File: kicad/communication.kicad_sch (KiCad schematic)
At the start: 5 parts

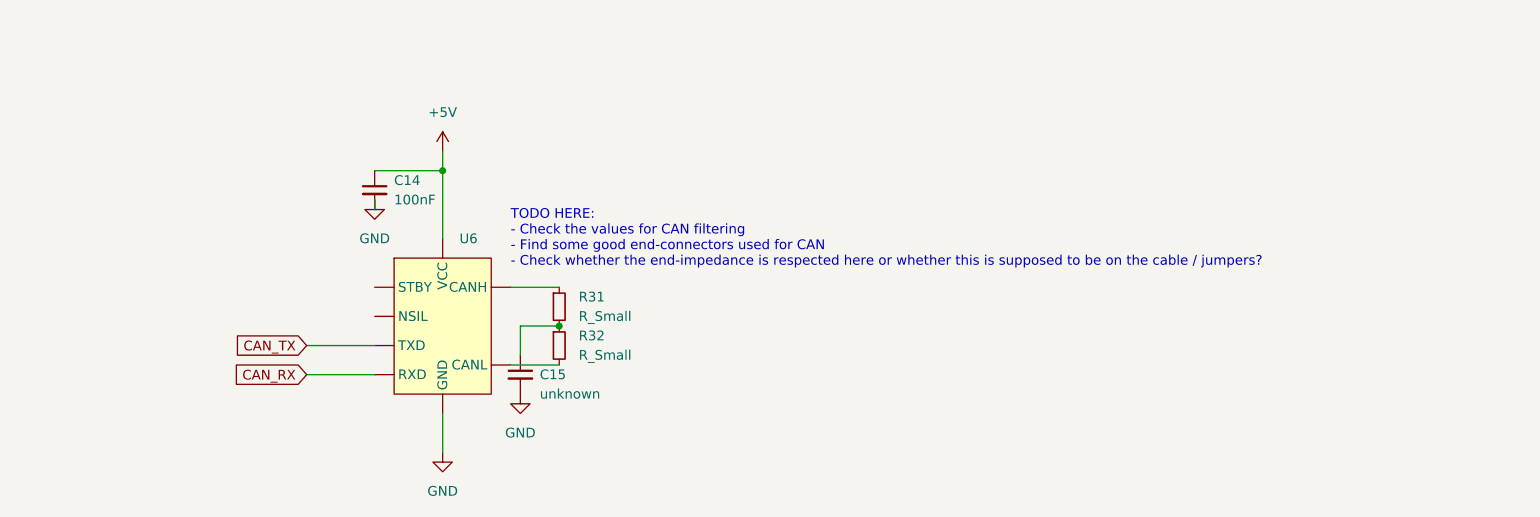
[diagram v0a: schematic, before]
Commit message: [kicad] Added end-connector and differential resistnace
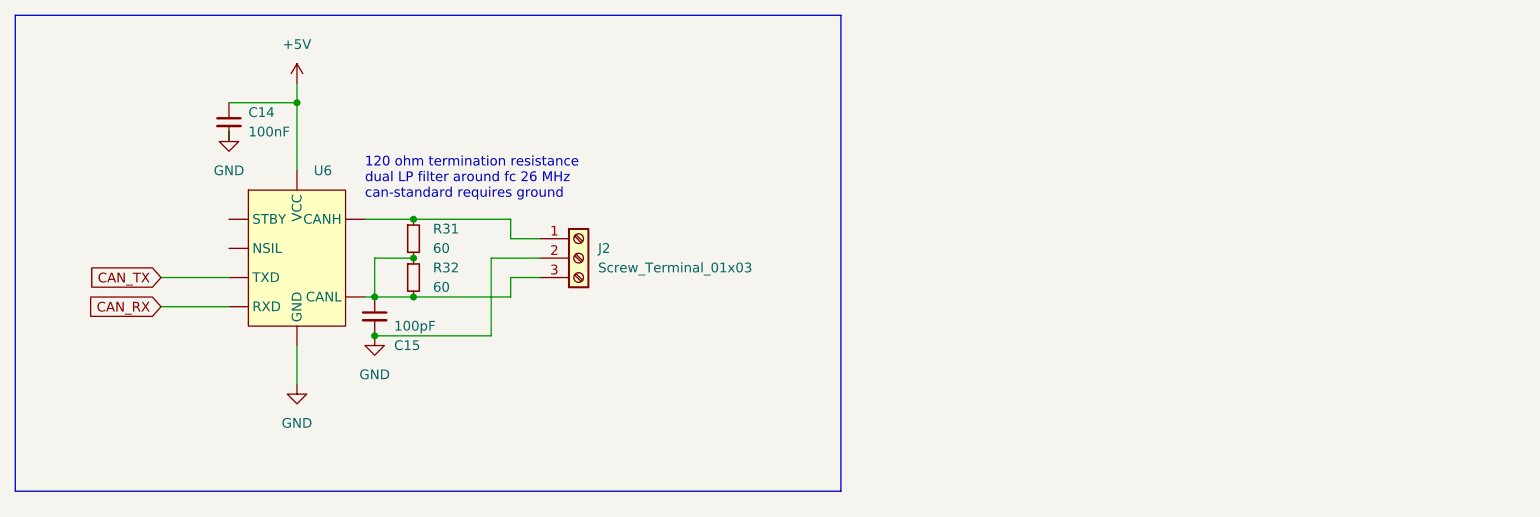
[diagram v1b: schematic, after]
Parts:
- added J2: Screw_Terminal_01x03, symbol Connector:Screw_Terminal_01x03
- C15: value unknown -> 100pF
- R31, R32: value R_Small -> 60
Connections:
- net GND: now also J2.2 (Pin_2)
- net at R31.1, U6. (VCC): now also J2.1 (Pin_1)
- net at C15.1, R31.2, R32.1: now also R32.2, U6. (VCC), J2.3 (Pin_3)
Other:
- note added: "120 ohm termination resistance dual LP filter around fc 26 MHz can-standard requires ground"
- note removed: "TODO HERE: - Check the values for CAN filtering - Find some good end-connectors used for CAN - Check whether the end-impedance is respected here or whether this is supposed to be on the cable / jumpers?"
- moved on the sheet: C14, C15, R31, R32, U6

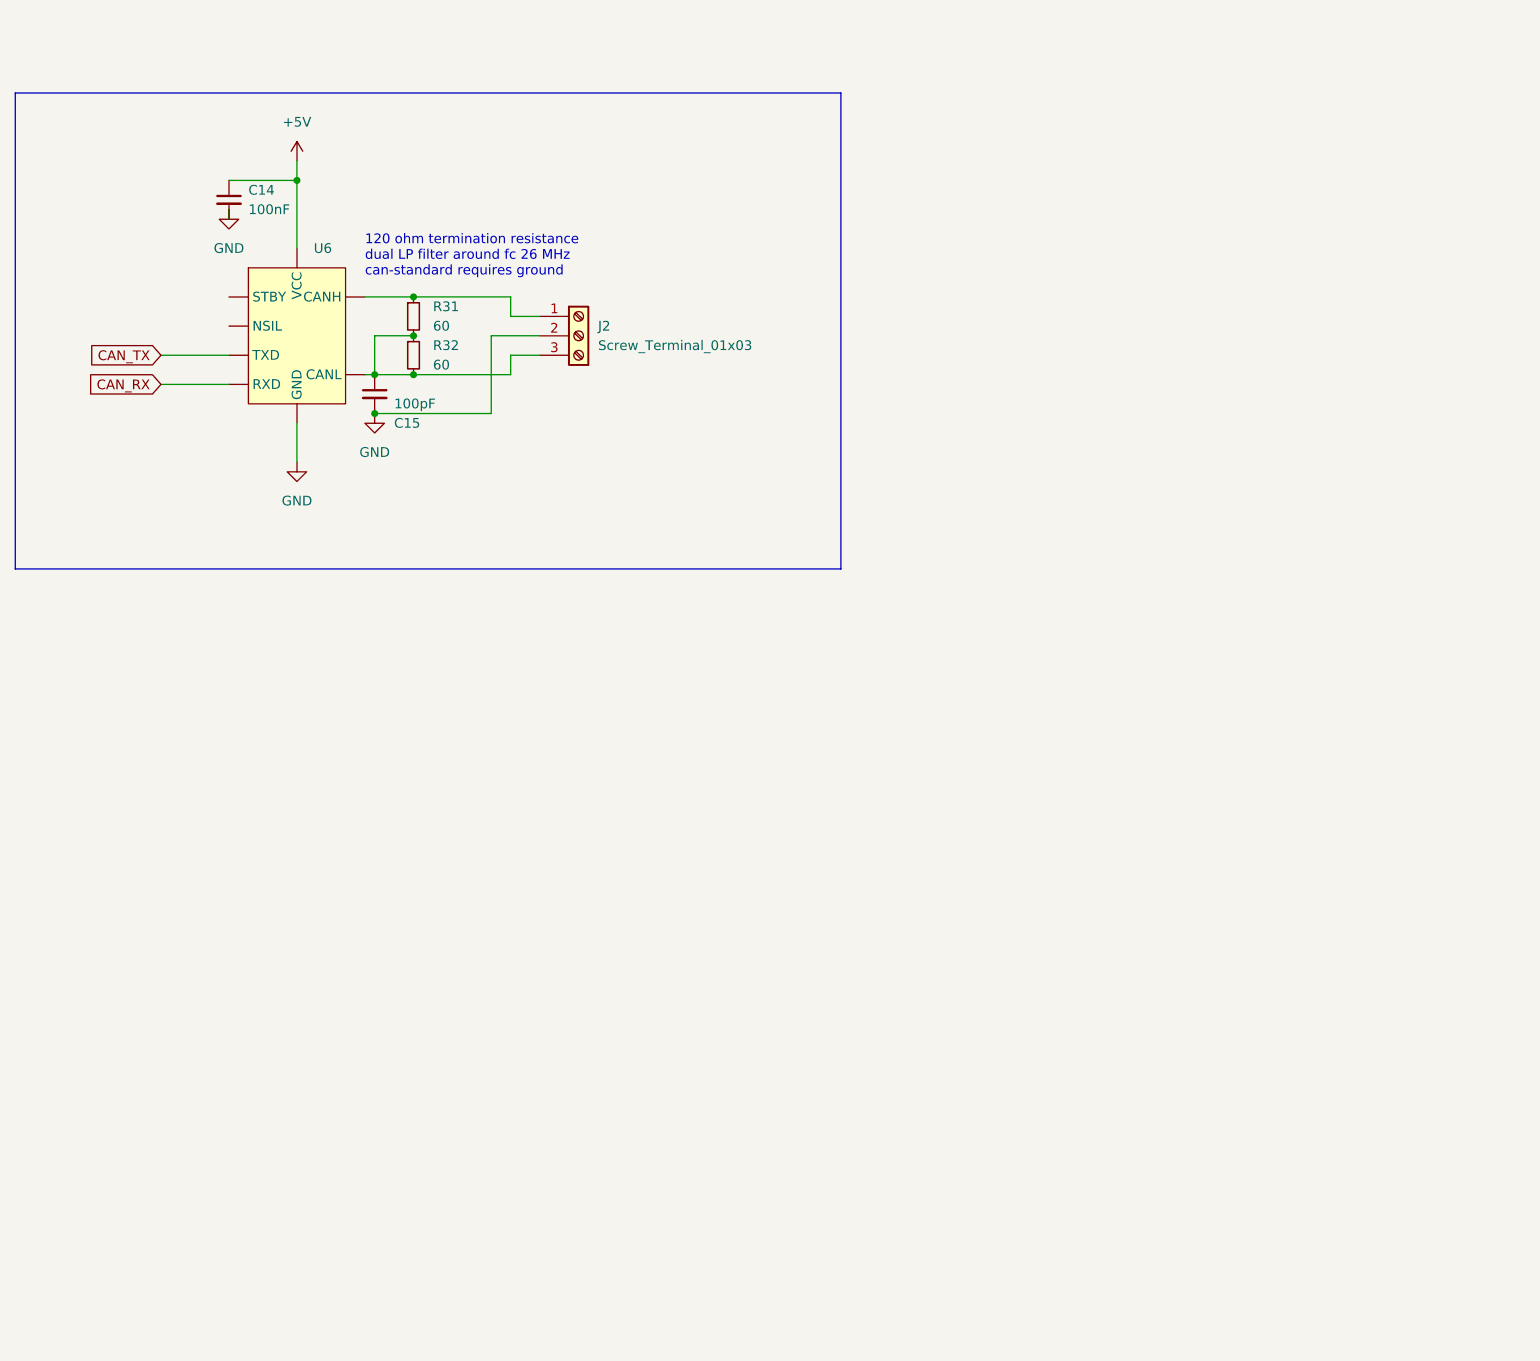
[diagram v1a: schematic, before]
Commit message: Changed USB configuration
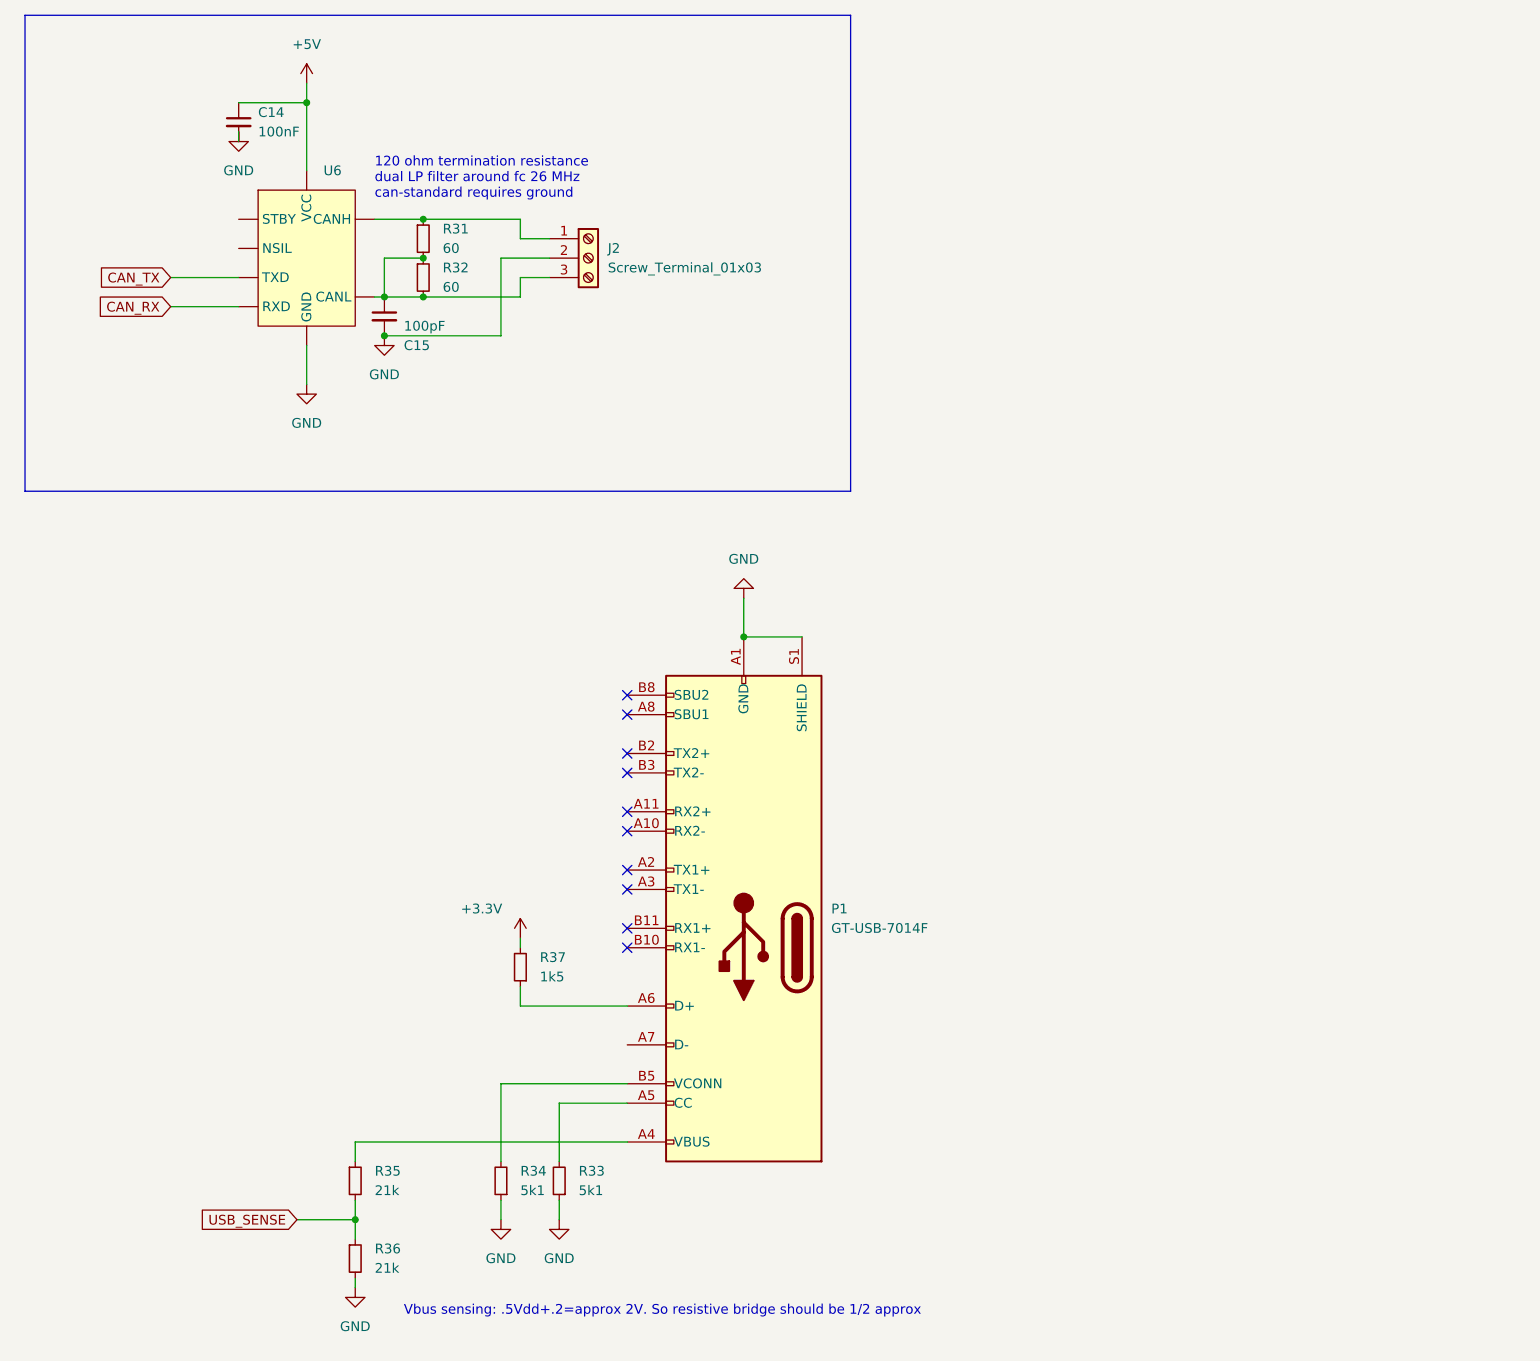
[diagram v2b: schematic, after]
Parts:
- added P1: GT-USB-7014F, symbol Connector:USB_C_Plug
- added R33, R34: 5k1, symbol Device:R_Small
- added R35, R36: 21k, symbol Device:R_Small
- added R37: 1k5, symbol Device:R_Small
- U6: JLPCB # (none) -> C2671262
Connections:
- net GND: now also P1.A1 (GND), P1.A12 (GND), P1.B1 (GND), P1.B12 (GND), P1.S1 (SHIELD), R33.1, R34.1, R36.2
- new net: P1.A4 (VBUS), P1.A9 (VBUS), P1.B4 (VBUS), P1.B9 (VBUS), R35.1
- new net: P1.A6 (D+), R37.1
- new net: P1.B5 (VCONN), R34.2
- new net: P1.A5 (CC), R33.2
- new net +3.3V: R37.2
- new net USB_SENSE: R35.2, R36.1
- no-connect marks 0 -> 10
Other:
- note added: "Vbus sensing: .5Vdd+.2=approx 2V. So resistive bridge should be 1/2 approx"
- moved on the sheet: C14, C15, J2, R31, R32, U6

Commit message: [kicad] Added i2c connection
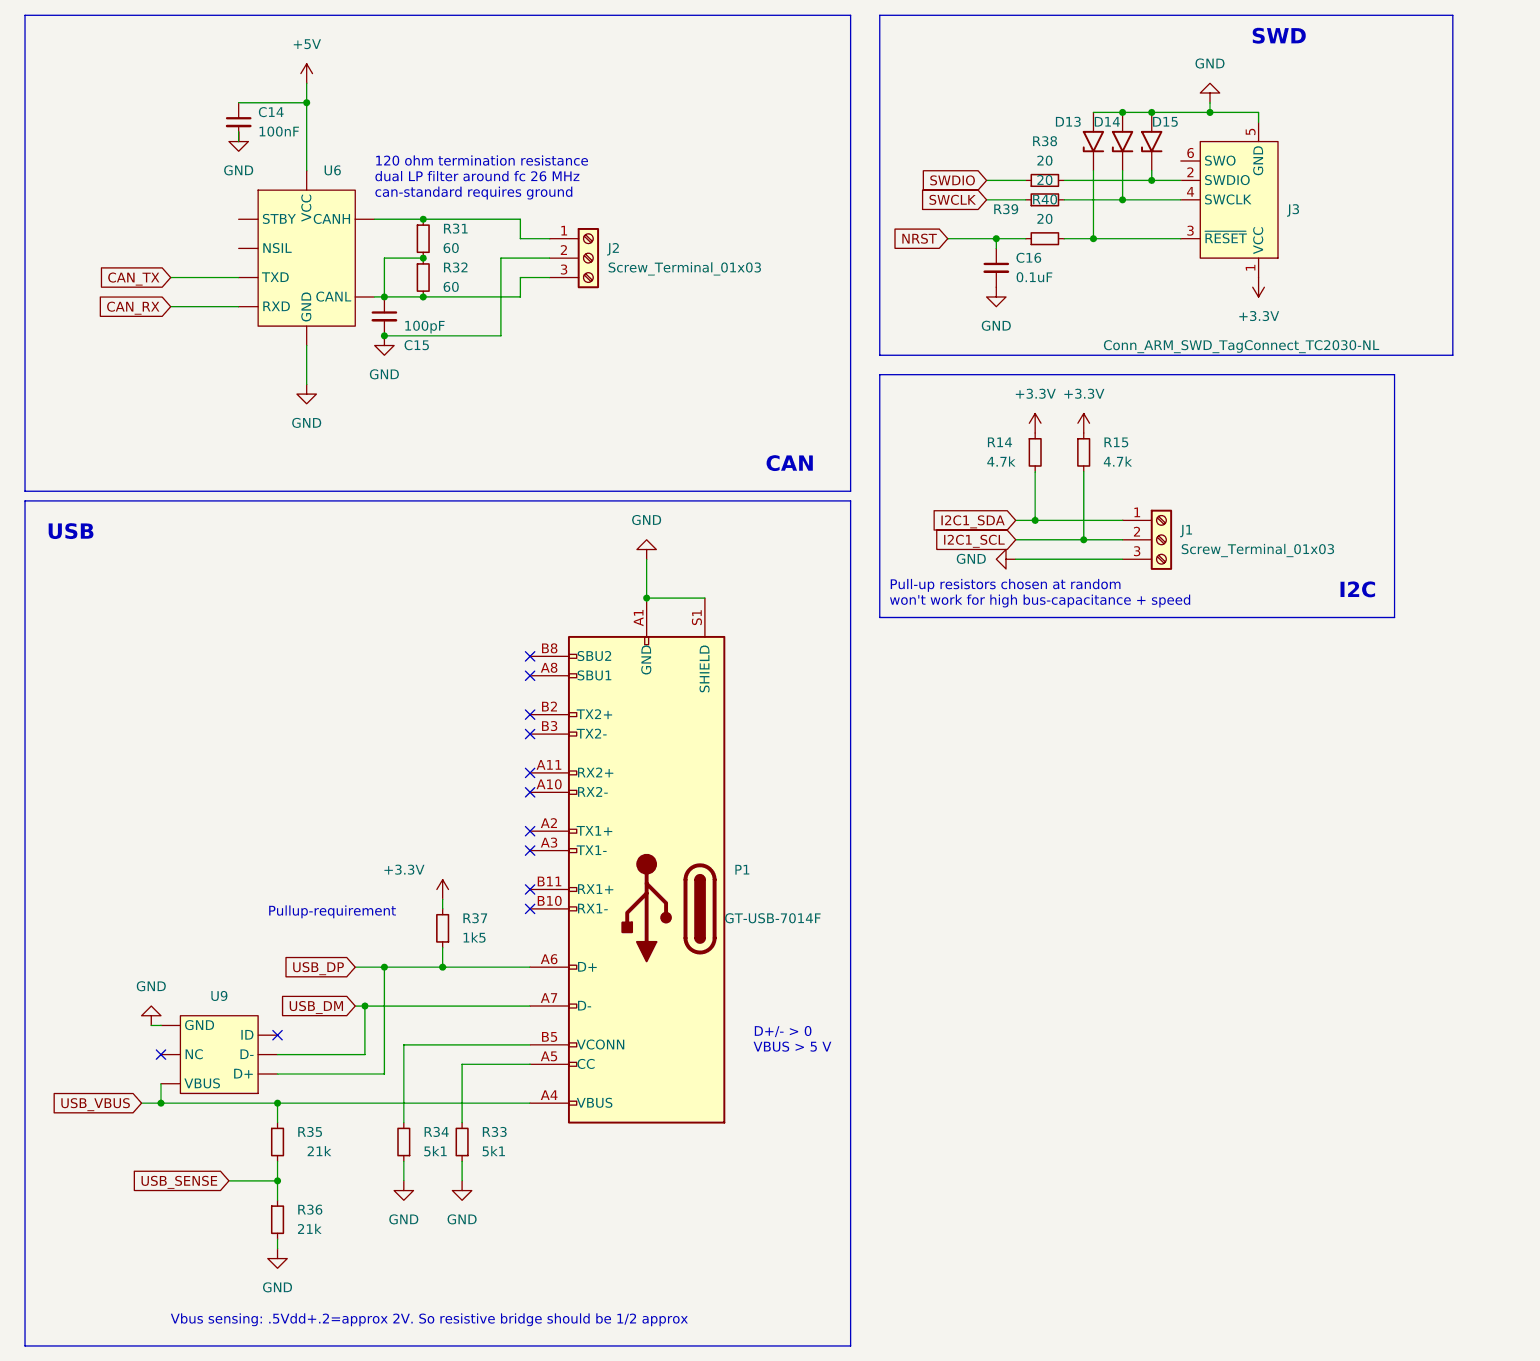
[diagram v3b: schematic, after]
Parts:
- added C16: 0.1uF, symbol Device:C_Small
- added D13, D14, D15: SMAJ13A, Diode_SMD:D_SMA, symbol Diode:SMAJ13A
- added J1: Screw_Terminal_01x03, symbol Connector:Screw_Terminal_01x03
- added J3: Conn_ARM_SWD_TagConnect_TC2030-NL, Connector:Tag-Connect_TC2030-IDC-NL_2x03_P1.27mm_Vertical, symbol Connector:Conn_ARM_SWD_TagConnect_TC2030-NL
- added R14, R15: 4.7k, symbol Device:R_Small
- added R38, R39, R40: 20, symbol Device:R_Small
- added U9: ~, symbol bldc:TPD4S012DRYR
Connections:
- net +3.3V: now also J3.1 (VCC), R14.1, R15.1
- net GND: now also C16.2, D13.2 (A2), D14.2 (A2), D15.2 (A2), J1.3 (Pin_3), J3.5 (GND), U9. (VBUS)
- net USB_VBUS: now reaches P1.A4 (VBUS), P1.A9 (VBUS), P1.B4 (VBUS), P1.B9 (VBUS), R35.1
- net USB_VBUS: now also U9. (VBUS)
- net USB_DP: now reaches P1.A6 (D+), R37.1
- net USB_DP: now also U9. (VBUS)
- net USB_DM: now reaches P1.A7 (D-)
- net USB_DM: now also U9. (VBUS)
- new net: D14.1 (A1), J3.4 (SWCLK), R39.2
- new net: D15.1 (A1), J3.2 (SWDIO), R38.2
- new net: D13.1 (A1), J3.3 (~{RESET}), R40.2
- new net I2C1_SCL: J1.2 (Pin_2), R15.2
- new net I2C1_SDA: J1.1 (Pin_1), R14.2
- new net NRST: C16.1, R40.1
- new net SWCLK: R39.1
- new net SWDIO: R38.1
- no-connect marks 10 -> 12
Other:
- note added: "D+/- > 0 VBUS > 5 V"
- note added: "Pull-up resistors chosen at random won't work for high bus-capacitance + speed"
- note added: "Pullup-requirement"
- moved on the sheet: P1, R33, R34, R35, R36, R37
